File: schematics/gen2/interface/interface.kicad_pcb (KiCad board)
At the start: 2 copper layers, 100 x 101.6 mm, 16 parts, among them U1 74LS00, U2 74LS00, U4 74LS245, U5 74LS193, U6 74LS193, U7 74LS193, U8 74LS193

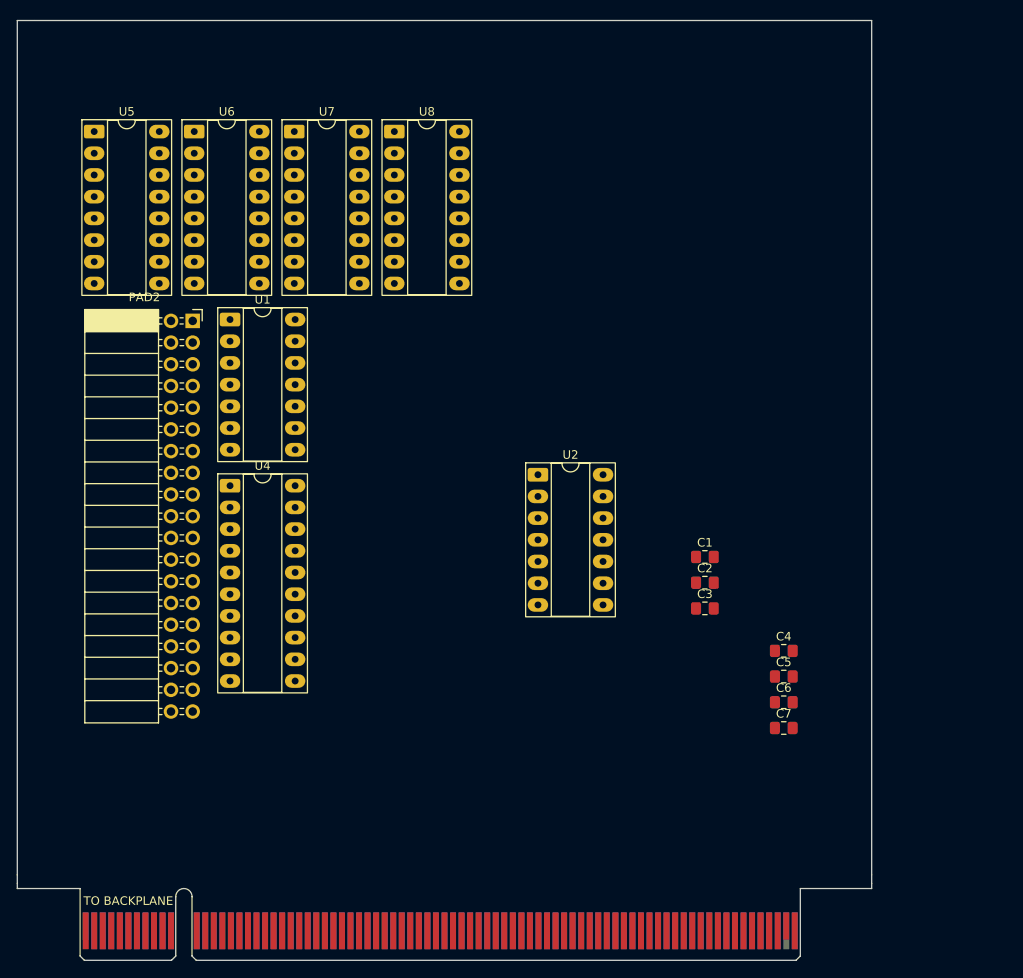
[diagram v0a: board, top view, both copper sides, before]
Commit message: Add interface module
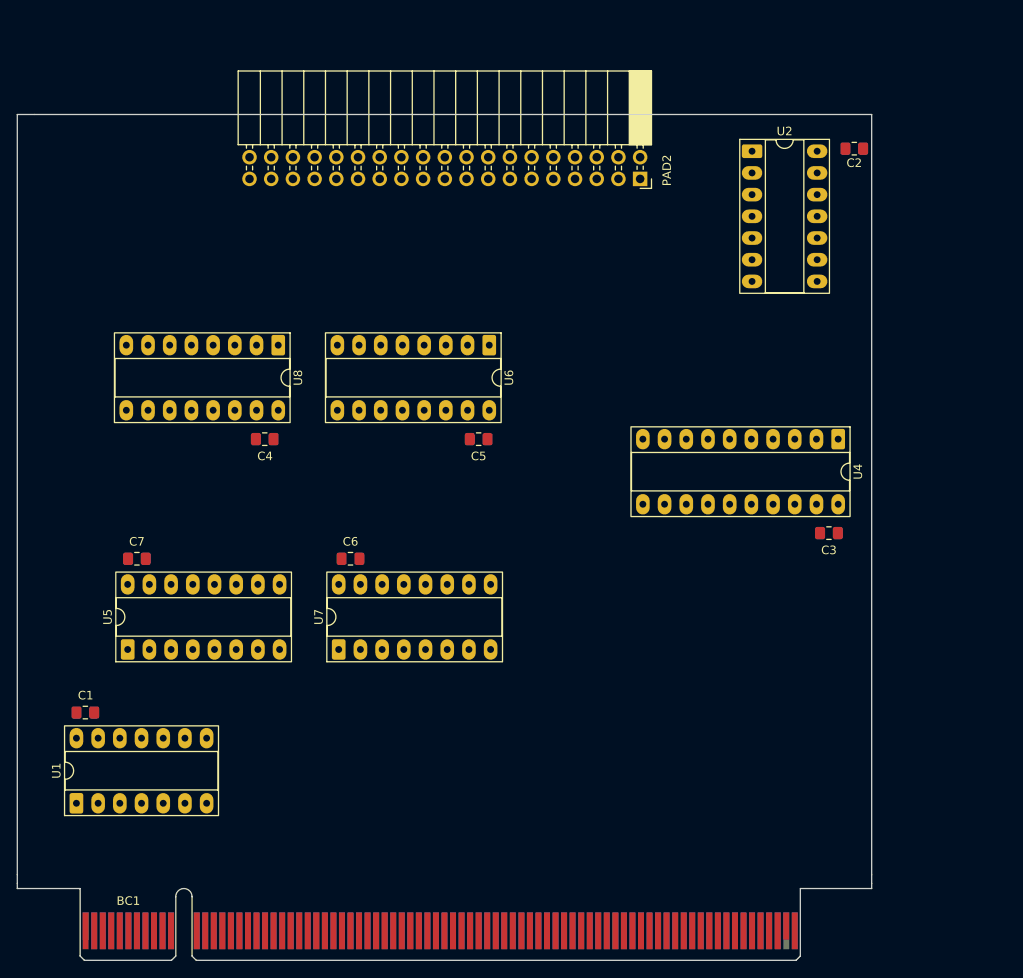
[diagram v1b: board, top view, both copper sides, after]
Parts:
- BC1: renamed from TO BACKPLANE
- moved C7 78.3 mm to (84.0, 86.0), turned to 180 degrees
- moved C1 74.8 mm to (78.0, 104.0), turned to 180 degrees
- moved U4 71.4 mm to (166.1, 72.0), turned to -90 degrees
- moved C4 65.6 mm to (99.0, 72.0)
- moved U7 60.8 mm to (107.6, 96.6), turned to 90 degrees
- moved U5 60.7 mm to (82.9, 96.6), turned to 90 degrees
- moved U1 59.4 mm to (76.9, 114.6), turned to 90 degrees
- moved PAD2 54.9 mm to (142.9, 41.5), turned to -90 degrees
- moved C2 53.7 mm to (168.0, 38.0), turned to 180 degrees
- moved C6 53.4 mm to (109.0, 86.0), turned to 180 degrees
- moved U2 45.4 mm to (156.0, 38.3)
- moved C5 45.3 mm to (124.0, 72.0)
- moved U6 42.6 mm to (125.2, 61.0), turned to -90 degrees
- moved U8 28.5 mm to (100.5, 61.0), turned to -90 degrees
- moved C3 17.0 mm to (165.0, 83.0)
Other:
- board size 100 x 101.6 mm -> 100 x 90.6 mm

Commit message: Implement code changes to enhance functionality and improve performance
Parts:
- added C8: C, Capacitor_THT:C_Radial_D6.3mm_H5.0mm_P2.50mm, F.Cu at (95.5, 107.8)
- C1, C2, C3, C4, C5, C6, C7: footprint Capacitor_SMD:C_0805_2012Metric_Pad1.18x1.45mm_HandSolder -> Capacitor_THT:C_Disc_D5.0mm_W2.5mm_P5.00mm
- moved U1 100.6 mm to (169.8, 76.1), turned to 0 degrees
- moved C7 97.7 mm to (181.2, 75.8), turned to -90 degrees
- moved C1 72.2 mm to (128.7, 52.6), turned to -90 degrees
- moved U5 61.8 mm to (143.4, 84.4)
- moved C2 60.7 mm to (139.0, 91.3), turned to -90 degrees
- moved C6 54.2 mm to (112.6, 31.9), turned to 0 degrees
- moved U4 52.7 mm to (116.9, 53.1), turned to 0 degrees
- moved U7 45.2 mm to (143.6, 69.3)
- moved U8 43.6 mm to (143.6, 54.2), turned to 90 degrees
- moved U2 43.2 mm to (113.1, 43.7), turned to 90 degrees
- moved U6 42.5 mm to (143.7, 99.3), turned to 90 degrees
- moved C4 41.2 mm to (138.8, 61.3), turned to -90 degrees
- moved PAD2 39.1 mm to (105.3, 52.3), turned to 0 degrees
- moved C5 29.7 mm to (138.7, 46.2), turned to -90 degrees
- moved C3 27.2 mm to (138.7, 76.2), turned to -90 degrees
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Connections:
- C1 pad 1: GND -> VCC
- C1 pad 2: VCC -> GND
- C2 pad 1: GND -> VCC
- C2 pad 2: VCC -> GND
- C3 pad 1: GND -> VCC
- C3 pad 2: VCC -> GND
- C4 pad 1: GND -> VCC
- C4 pad 2: VCC -> GND
- C5 pad 1: GND -> VCC
- C5 pad 2: VCC -> GND
- C6 pad 1: GND -> VCC
- C6 pad 2: VCC -> GND
- C7 pad 1: GND -> VCC
- C7 pad 2: VCC -> GND
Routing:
- net /BUS4: track 0.00 -> 58.4 mm
- net /BUS3: track 0.00 -> 32.3 mm
- net /BUS2: track 0.00 -> 31.6 mm
- net /BUS0: track 0.00 -> 28.6 mm, vias 0 -> 1
- net /BUS1: track 0.00 -> 22.2 mm
- added copper zone on B.Cu, net GND
- added copper zone on F.Cu, net VCC
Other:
- board size 100 x 90.6 mm -> 100 x 91 mm

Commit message: inprogress(interface): 19 pins left
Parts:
- moved C6 1.28 mm to (113.7, 32.6)
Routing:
- net /~{Wait}: track 0.00 -> 220.0 mm, vias 0 -> 4
- net /IntReq: track 0.00 -> 215.2 mm, vias 0 -> 4
- net /~{Clk}: track 0.00 -> 190.4 mm, vias 0 -> 2
- net /Reset: track 0.00 -> 173.6 mm, vias 0 -> 8
- net /ADDRESS0: track 0.00 -> 132.5 mm, vias 0 -> 5
- net /ADDRESS3: track 0.00 -> 131.9 mm, vias 0 -> 6
- net /ADDRESS2: track 0.00 -> 127.9 mm, vias 0 -> 4
- net GND: track 0.45 -> 127.3 mm, vias 0 -> 8
- net /BUS3: track 32.3 -> 135.3 mm, vias 0 -> 5
- net /BUS2: track 31.6 -> 129.8 mm, vias 0 -> 5
- net /~{MemWrite}: track 0.00 -> 96.9 mm, vias 0 -> 4
- net /~{MemRead}: track 0.00 -> 94.9 mm, vias 0 -> 4
- net /AddrLowIn: track 0.00 -> 93.0 mm, vias 0 -> 4
- net /~{IntAck}: track 0.00 -> 87.7 mm, vias 0 -> 2
- net /AddrHighIn: track 0.00 -> 86.2 mm, vias 0 -> 4
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
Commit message: done(interface)
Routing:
- net /ADDRESS14: track 0.00 -> 262.7 mm, vias 0 -> 12
- net /ADDRESS15: track 0.00 -> 244.4 mm, vias 0 -> 9
- net /ADDRESS11: track 0.00 -> 229.3 mm, vias 0 -> 5
- net /ADDRESS12: track 0.00 -> 218.9 mm, vias 0 -> 6
- net /ADDRESS7: track 0.00 -> 195.0 mm, vias 0 -> 8
- net /ADDRESS6: track 0.00 -> 181.1 mm, vias 0 -> 8
- net Net-(U6-UP): track 0.00 -> 138.9 mm, vias 0 -> 14
- net /BUS7: track 65.3 -> 178.5 mm, vias 1 -> 11
- net /ADDRESS10: track 0.00 -> 100.0 mm, vias 0 -> 3
- net /ADDRESS8: track 0.00 -> 54.7 mm, vias 0 -> 4
- net /ADDRESS4: track 0.00 -> 53.9 mm, vias 0 -> 5
- net /ADDRESS13: track 0.00 -> 52.0 mm, vias 0 -> 5
- net /ADDRESS5: track 0.00 -> 50.0 mm, vias 0 -> 4
- net /ADDRESS9: track 0.00 -> 46.6 mm, vias 0 -> 3
- net Net-(U6-DOWN): track 0.00 -> 38.9 mm, vias 0 -> 1
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
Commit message: interface review
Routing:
- net /ADDRESS10: track 100.0 -> 64.8 mm, vias 3 -> 5
- net /ADDRESS14: track 262.7 -> 264.3 mm
- net /~{Wait}: track 220.0 -> 221.6 mm
- net Net-(U6-UP): track 138.9 -> 140.1 mm
- net /IntReq: track 215.2 -> 216.2 mm
- net /Pulse: track 70.3 -> 69.5 mm
- net /ADDRESS7: track 195.0 -> 195.6 mm
- net /ADDRESS6: track 181.1 -> 181.8 mm
- net /ADDRESS12: track 218.9 -> 219.6 mm
- net /ADDRESS11: track 229.3 -> 230.0 mm
